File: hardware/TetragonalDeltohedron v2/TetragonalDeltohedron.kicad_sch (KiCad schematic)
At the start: 111 parts, among them J1 Conn_01x04, U1 XL-0807RGBC-WS2812B, U10 XL-0807RGBC-WS2812B, U2 XL-0807RGBC-WS2812B, U3 XL-0807RGBC-WS2812B, U4 XL-0807RGBC-WS2812B, U5 XL-0807RGBC-WS2812B, U6 XL-0807RGBC-WS2812B, U7 XL-0807RGBC-WS2812B, U8 XL-0807RGBC-WS2812B, U9 XL-0807RGBC-WS2812B

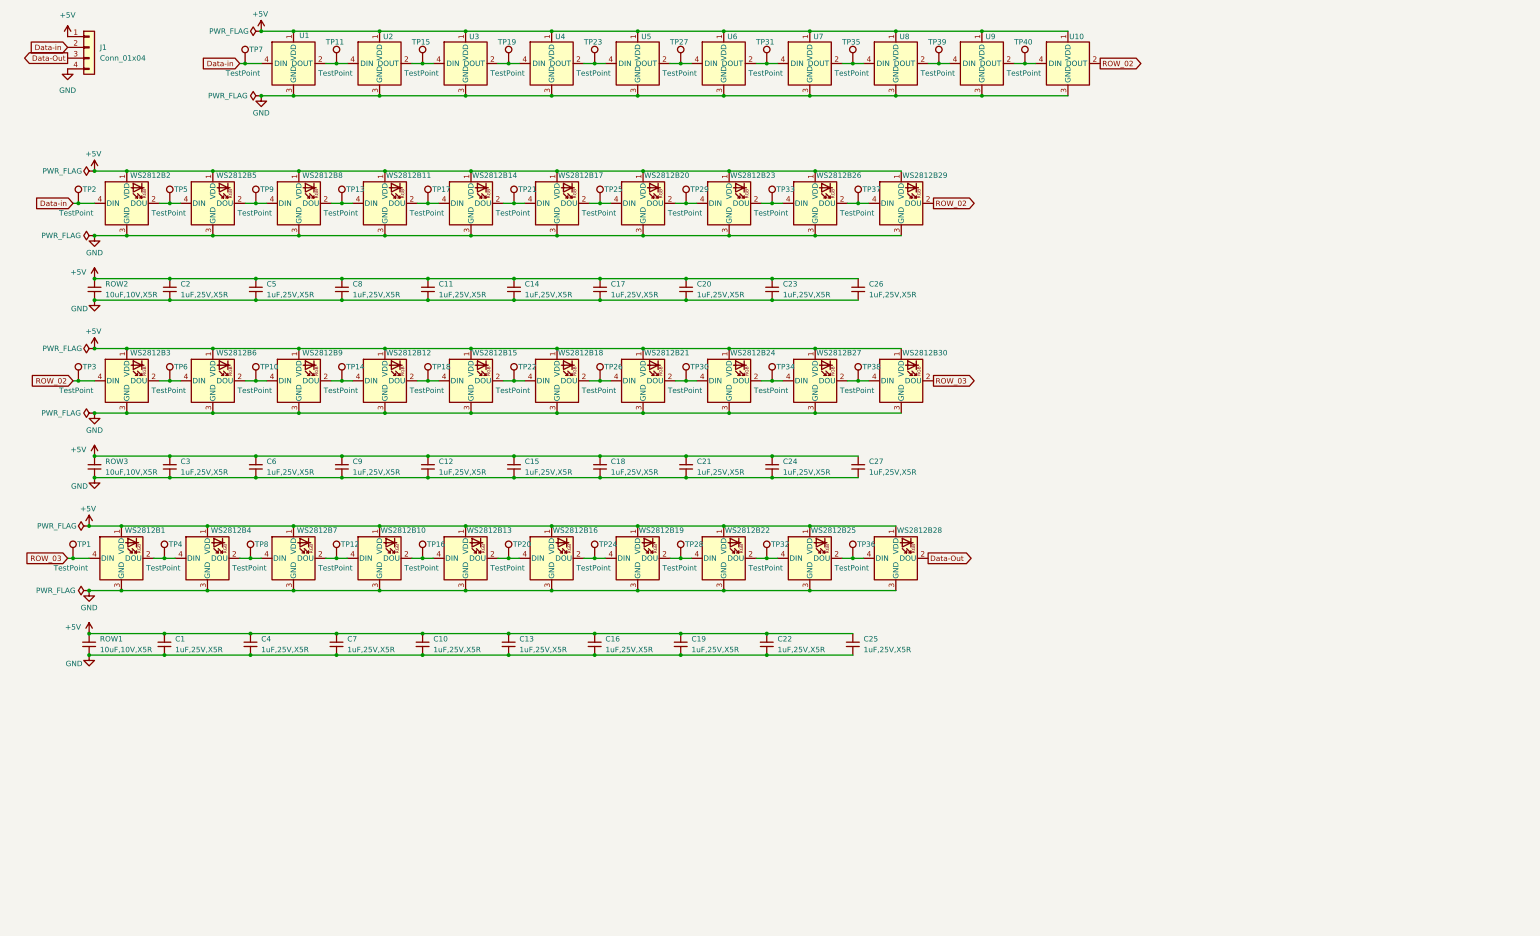
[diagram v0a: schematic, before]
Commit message: Adding all the components to the PCB
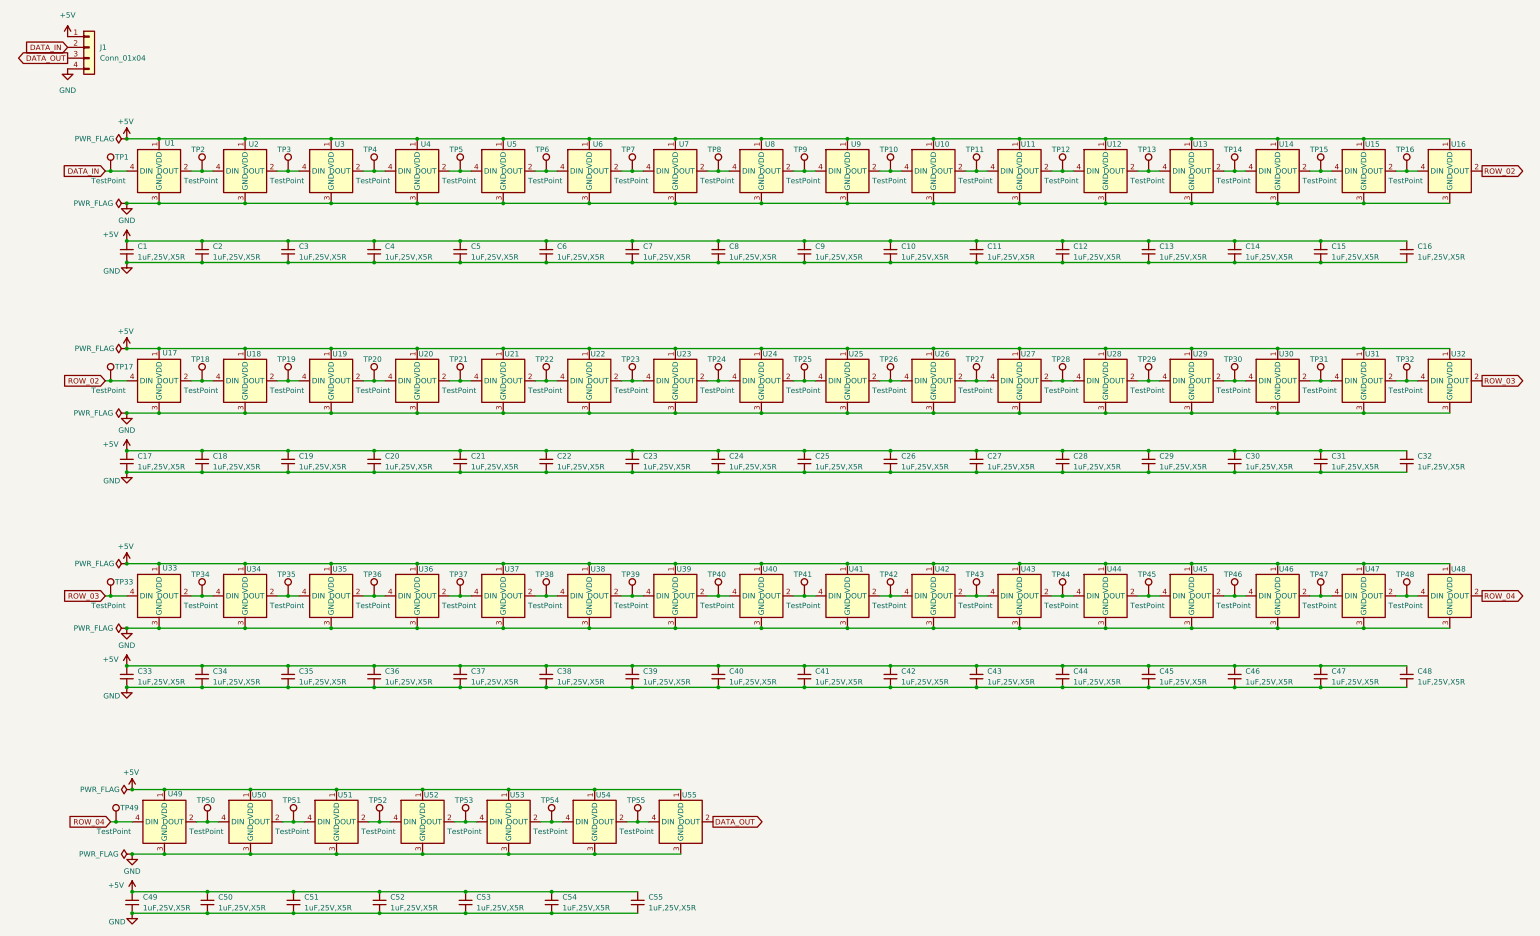
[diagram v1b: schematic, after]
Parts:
- removed C10, C3, C4, C6, C7, C9: 1uF,25V,X5R, SWS-Library:C_0402_1005Metric, symbol __sws_jlpcb:jlcpcb-1uF,25V,X5R
- removed ROW1, ROW2, ROW3: 10uF,10V,X5R, SWS-Library:C_0402_1005Metric, symbol __sws_jlpcb:jlcpcb-1uF,25V,X5R
- removed TP1, TP10, TP2, TP3, TP4, TP5, TP6, TP8, TP9: TestPoint, symbol Connector:TestPoint
- removed WS2812B1, WS2812B10, WS2812B11, WS2812B12, WS2812B13, WS2812B14, WS2812B15, WS2812B16, WS2812B17, WS2812B18, WS2812B19, WS2812B2, WS2812B20, WS2812B21, WS2812B22, WS2812B23, WS2812B24, WS2812B25, WS2812B26, WS2812B27, WS2812B28, WS2812B29, WS2812B3, WS2812B30, WS2812B4, WS2812B5, WS2812B6, WS2812B7, WS2812B8, WS2812B9: XL-5050RGBC-WS2812B, LED_SMD:LED_WS2812B_PLCC4_5.0x5.0mm_P3.2mm, symbol __sws_jlpcb:XL-5050RGBC-WS2812B
- added C11, C14, C17, C20, C23, C26, C28, C29, C30, C31, C32, C33, C34, C35, C36, C37, C38, C39, C40, C41, C42, C43, C44, C45, C46, C47, C48, C49, C50, C51, C52, C53, C54, C55: 1uF,25V,X5R, SWS-Library:C_0402_1005Metric, symbol __sws_jlpcb:jlcpcb-1uF,25V,X5R
- added TP11, TP15, TP19, TP23, TP27, TP31, TP35, TP39, TP40, TP41, TP42, TP43, TP44, TP45, TP46, TP47, TP48, TP49, TP50, TP51, TP52, TP53, TP54, TP55: TestPoint, symbol Connector:TestPoint
- added U11, U12, U13, U14, U15, U16, U17, U18, U19, U20, U21, U22, U23, U24, U25, U26, U27, U28, U29, U30, U31, U32, U33, U34, U35, U36, U37, U38, U39, U40, U41, U42, U43, U44, U45, U46, U47, U48, U49, U50, U51, U52, U53, U54, U55: XL-0807RGBC-WS2812B, SWS-Library:XL-0807RGBC-WS2812B, symbol __sws_jlpcb:XL-0807RGBC-WS2812B
- renumbered C26 to C10, C5 to C3, C8 to C4, C11 to C5, C14 to C6, C17 to C7, C20 to C8, C23 to C9, TP7 to TP1, TP40 to TP10, TP11 to TP2, TP15 to TP3, TP19 to TP4, TP23 to TP5, TP27 to TP6, TP31 to TP7, TP35 to TP8, TP39 to TP9
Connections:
- net +5V: now also C11.1, C14.1, C17.1, C20.1, C23.1, C26.1, C28.1, C29.1, C30.1, C31.1, C32.1, C33.1, C34.1, C35.1, C36.1, C37.1, C38.1, C39.1, C40.1, C41.1, C42.1, C43.1, C44.1, C45.1, C46.1, C47.1, C48.1, C49.1, C50.1, C51.1, C52.1, C53.1, C54.1, C55.1, U11.1 (VDD), U12.1 (VDD), U13.1 (VDD), U14.1 (VDD), U15.1 (VDD), U16.1 (VDD), U17.1 (VDD), U18.1 (VDD), U19.1 (VDD), U20.1 (VDD), U21.1 (VDD), U22.1 (VDD), U23.1 (VDD), U24.1 (VDD), U25.1 (VDD), U26.1 (VDD), U27.1 (VDD), U28.1 (VDD), U29.1 (VDD), U30.1 (VDD), U31.1 (VDD), U32.1 (VDD), U33.1 (VDD), U34.1 (VDD), U35.1 (VDD), U36.1 (VDD), U37.1 (VDD), U38.1 (VDD), U39.1 (VDD), U40.1 (VDD), U41.1 (VDD), U42.1 (VDD), U43.1 (VDD), U44.1 (VDD), U45.1 (VDD), U46.1 (VDD), U47.1 (VDD), U48.1 (VDD), U49.1 (VDD), U50.1 (VDD), U51.1 (VDD), U52.1 (VDD), U53.1 (VDD), U54.1 (VDD), U55.1 (VDD)
- net GND: now also C11.2, C14.2, C17.2, C20.2, C23.2, C26.2, C28.2, C29.2, C30.2, C31.2, C32.2, C33.2, C34.2, C35.2, C36.2, C37.2, C38.2, C39.2, C40.2, C41.2, C42.2, C43.2, C44.2, C45.2, C46.2, C47.2, C48.2, C49.2, C50.2, C51.2, C52.2, C53.2, C54.2, C55.2, U11.3 (GND), U12.3 (GND), U13.3 (GND), U14.3 (GND), U15.3 (GND), U16.3 (GND), U17.3 (GND), U18.3 (GND), U19.3 (GND), U20.3 (GND), U21.3 (GND), U22.3 (GND), U23.3 (GND), U24.3 (GND), U25.3 (GND), U26.3 (GND), U27.3 (GND), U28.3 (GND), U29.3 (GND), U30.3 (GND), U31.3 (GND), U32.3 (GND), U33.3 (GND), U34.3 (GND), U35.3 (GND), U36.3 (GND), U37.3 (GND), U38.3 (GND), U39.3 (GND), U40.3 (GND), U41.3 (GND), U42.3 (GND), U43.3 (GND), U44.3 (GND), U45.3 (GND), U46.3 (GND), U47.3 (GND), U48.3 (GND), U49.3 (GND), U50.3 (GND), U51.3 (GND), U52.3 (GND), U53.3 (GND), U54.3 (GND), U55.3 (GND)
- net ROW_02: now also TP17.1, U16.2 (DOUT), U17.4 (DIN); no longer U10.2 (DOUT)
- net ROW_03: now also TP33.1, U32.2 (DOUT), U33.4 (DIN)
- net at TP37.1: now also U36.2 (DOUT), U37.4 (DIN)
- net at TP22.1: now also U21.2 (DOUT), U22.4 (DIN)
- net at TP18.1: now also U17.2 (DOUT), U18.4 (DIN)
- net at TP38.1: now also U37.2 (DOUT), U38.4 (DIN)
- net at TP36.1: now also U35.2 (DOUT), U36.4 (DIN)
- net at TP32.1: now also U31.2 (DOUT), U32.4 (DIN)
- net at TP28.1: now also U27.2 (DOUT), U28.4 (DIN)
- net at TP34.1: now also U33.2 (DOUT), U34.4 (DIN)
- net at TP24.1: now also U23.2 (DOUT), U24.4 (DIN)
- net at TP12.1: now also U11.2 (DOUT), U12.4 (DIN)
- net at TP29.1: now also U28.2 (DOUT), U29.4 (DIN)
- net at TP26.1: now also U25.2 (DOUT), U26.4 (DIN)
- net at TP16.1: now also U15.2 (DOUT), U16.4 (DIN)
- net at TP30.1: now also U29.2 (DOUT), U30.4 (DIN)
- net at TP21.1: now also U20.2 (DOUT), U21.4 (DIN)
- net at TP20.1: now also U19.2 (DOUT), U20.4 (DIN)
- net at TP25.1: now also U24.2 (DOUT), U25.4 (DIN)
- net at TP13.1: now also U12.2 (DOUT), U13.4 (DIN)
- net at TP14.1: now also U13.2 (DOUT), U14.4 (DIN)
- net Data-Out renamed DATA_OUT
- net DATA_OUT: now also U55.2 (DOUT)
- net Data-in renamed DATA_IN
- new net: TP19.1, U18.2 (DOUT), U19.4 (DIN)
- new net: TP11.1, U10.2 (DOUT), U11.4 (DIN)
- new net: TP23.1, U22.2 (DOUT), U23.4 (DIN)
- new net: TP44.1, U43.2 (DOUT), U44.4 (DIN)
- new net: TP43.1, U42.2 (DOUT), U43.4 (DIN)
- new net: TP15.1, U14.2 (DOUT), U15.4 (DIN)
- new net: TP51.1, U50.2 (DOUT), U51.4 (DIN)
- new net: TP50.1, U49.2 (DOUT), U50.4 (DIN)
- new net: TP27.1, U26.2 (DOUT), U27.4 (DIN)
- new net: TP46.1, U45.2 (DOUT), U46.4 (DIN)
- new net: TP45.1, U44.2 (DOUT), U45.4 (DIN)
- new net: TP31.1, U30.2 (DOUT), U31.4 (DIN)
- new net: TP47.1, U46.2 (DOUT), U47.4 (DIN)
- new net: TP40.1, U39.2 (DOUT), U40.4 (DIN)
- new net: TP55.1, U54.2 (DOUT), U55.4 (DIN)
- new net: TP54.1, U53.2 (DOUT), U54.4 (DIN)
- new net: TP53.1, U52.2 (DOUT), U53.4 (DIN)
- new net: TP42.1, U41.2 (DOUT), U42.4 (DIN)
- new net: TP41.1, U40.2 (DOUT), U41.4 (DIN)
- new net: TP39.1, U38.2 (DOUT), U39.4 (DIN)
- new net: TP52.1, U51.2 (DOUT), U52.4 (DIN)
- new net: TP35.1, U34.2 (DOUT), U35.4 (DIN)
- new net: TP48.1, U47.2 (DOUT), U48.4 (DIN)
- new net ROW_04: TP49.1, U48.2 (DOUT), U49.4 (DIN)
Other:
- moved on the sheet: C10, C2, C3, C4, C5, C6, C7, C8, C9, TP1, TP10, TP2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
